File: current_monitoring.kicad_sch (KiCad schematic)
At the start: 0 parts

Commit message: moving laptops
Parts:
- added R37: 28m, symbol Device:R
- added R38: 53m, symbol Device:R
- added R39: 1.1k, symbol Device:R
- added R40: 2.4k, symbol Device:R
- added U2: INA2180, symbol utsvt-chips:INA2180
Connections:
- net 12V_IN: now also R37.1, U2.2 (IN-)
- net 5V_IN: now also R38.1, U2.6 (IN-)
- new net: R39.1, U2.1 (OUT)
- new net: R39.2, R40.1
- new net 12V_LOAD: R37.2, U2.3 (IN+)
- new net 5V_LOAD: R38.2, U2.5 (IN+), U2.8 (VS), U2.8 (VS)
- new net GND: R40.2, U2.4 (GND), U2.4 (GND)

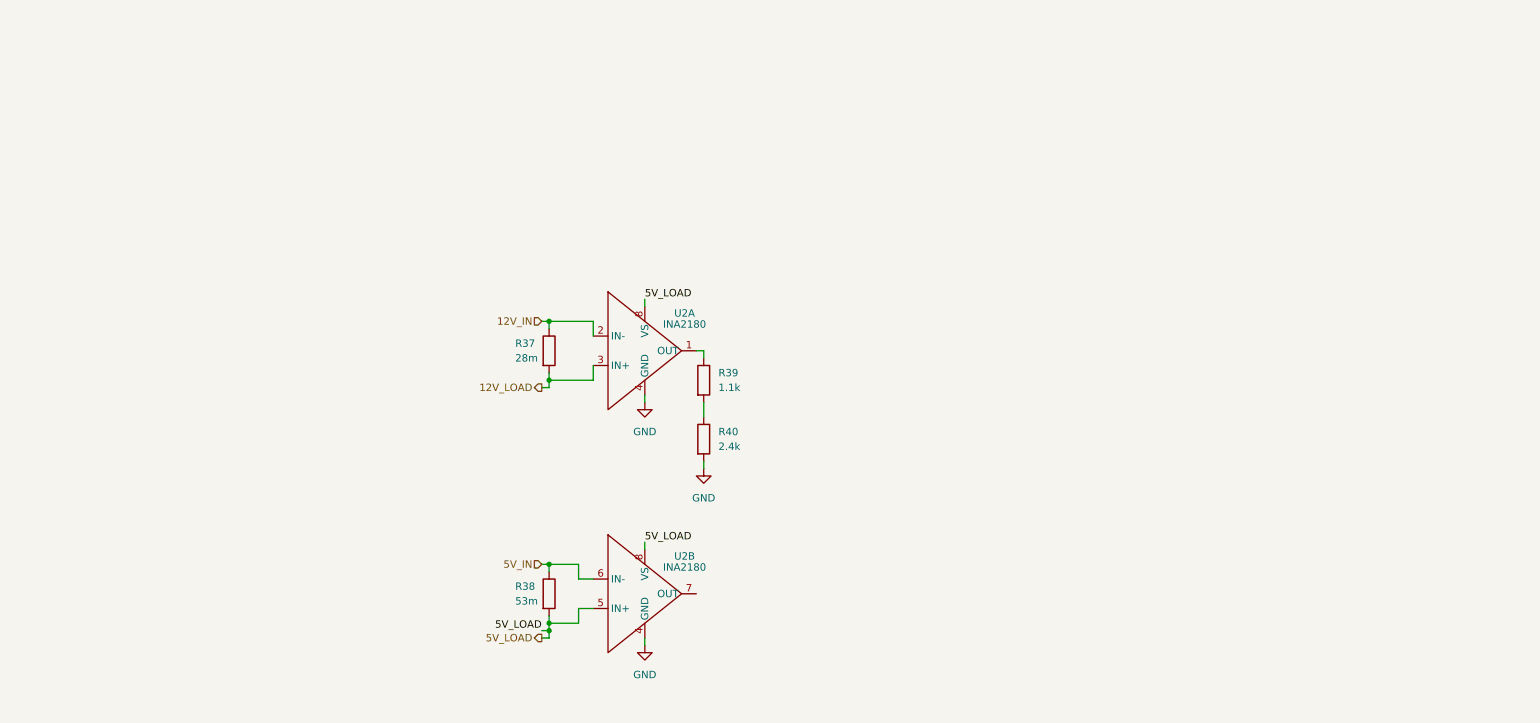
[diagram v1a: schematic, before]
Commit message: initial draft w/ current sense for 5V
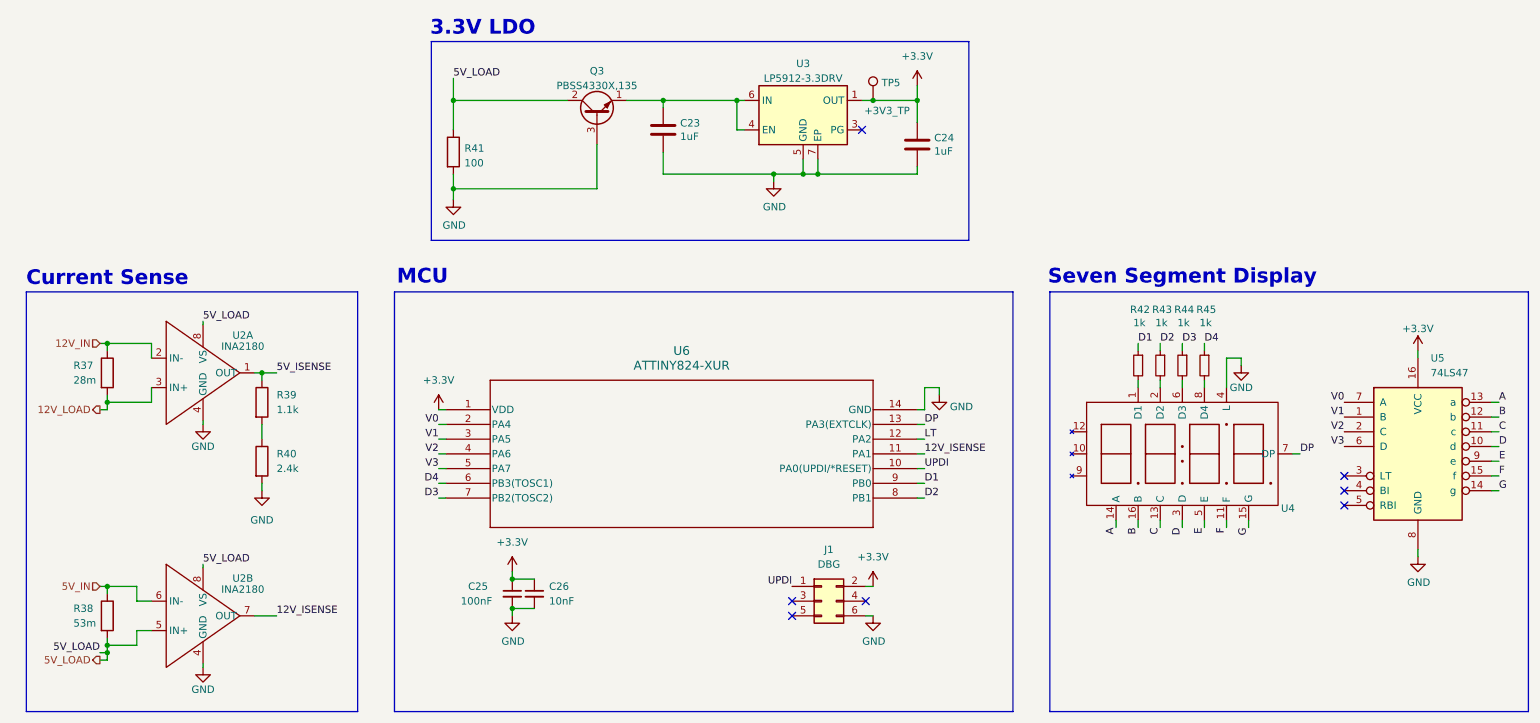
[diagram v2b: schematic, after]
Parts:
- added C23, C24: 1uF, Capacitor_SMD:C_0805_2012Metric, symbol Device:C
- added C25: 100nF, symbol Device:C_Small
- added C26: 10nF, symbol Device:C_Small
- added J1: DBG, symbol Connector_Generic:Conn_02x03_Odd_Even
- added Q3: PBSS4330X,135, Package_TO_SOT_SMD:SOT-89-3, symbol Transistor_BJT:2SC1815
- added R41: 100, Resistor_SMD:R_0805_2012Metric, symbol Device:R
- added R42, R43, R44, R45: 1k, symbol Device:R_Small
- added TP5: +3V3_TP, Connector_PinHeader_2.54mm:PinHeader_1x01_P2.54mm_Vertical, symbol Connector:TestPoint
- added U3: LP5912-3.3DRV, Package_SON:WSON-6-1EP_2x2mm_P0.65mm_EP1x1.6mm, symbol Regulator_Linear:LP5912-3.3DRV
- added U4: ~, symbol utsvt-misc:LTC-4627JS
- added U5: 74LS47, symbol 74xx:74LS47
- added U6: ATTINY824-XUR, TSSOP14_ST_MCH, symbol utsvt-microcontrollers:ATTINY824-XUR
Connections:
- net 5V_LOAD: now also Q3.2 (C), R41.1
- net GND: now also C23.2, C24.2, C25.2, C26.2, J1.6 (Pin_6), Q3.3 (B), R41.2, U3.5 (GND), U3.7 (EP), U4.4 (L), U5.8 (GND), U6.14 (GND)
- net 5V_ISENSE: now reaches R39.1, U2.1 (OUT)
- net 12V_ISENSE: now reaches U2.7 (OUT)
- net 12V_ISENSE: now also U6.11 (PA1)
- new net: R42.2, U4.1 (D1)
- new net: R43.2, U4.2 (D2)
- new net: R44.2, U4.6 (D3)
- new net: R45.2, U4.8 (D4)
- new net: C23.1, Q3.1 (E), U3.4 (EN), U3.6 (IN)
- new net +3.3V: C24.1, C25.1, C26.1, J1.2 (Pin_2), TP5.1, U3.1 (OUT), U5.16 (VCC), U6.1 (VDD)
- new net A: U4.14 (A), U5.13 (a)
- new net B: U4.16 (B), U5.12 (b)
- new net C: U4.13 (C), U5.11 (c)
- new net D: U4.3 (D), U5.10 (d)
- new net D1: R42.1, U6.9 (PB0)
- new net D2: R43.1, U6.8 (PB1)
- new net D3: R44.1, U6.7 (PB2(TOSC2))
- new net D4: R45.1, U6.6 (PB3(TOSC1))
- new net DP: U4.7 (DP), U6.13 (PA3(EXTCLK))
- new net E: U4.5 (E), U5.9 (e)
- new net F: U4.11 (F), U5.15 (f)
- new net G: U4.15 (G), U5.14 (g)
- new net LT: U6.12 (PA2)
- new net UPDI: J1.1 (Pin_1), U6.10 (PA0(UPDI/*RESET))
- new net V0: U5.7 (A), U6.2 (PA4)
- new net V1: U5.1 (B), U6.3 (PA5)
- new net V2: U5.2 (C), U6.4 (PA6)
- new net V3: U5.6 (D), U6.5 (PA7)
- no-connect marks 0 -> 7
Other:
- note added: "3.3V LDO"
- note added: "Current Sense"
- note added: "MCU"
- note added: "Seven Segment Display"
- moved on the sheet: R37, R38, R39, R40, U2A, U2B

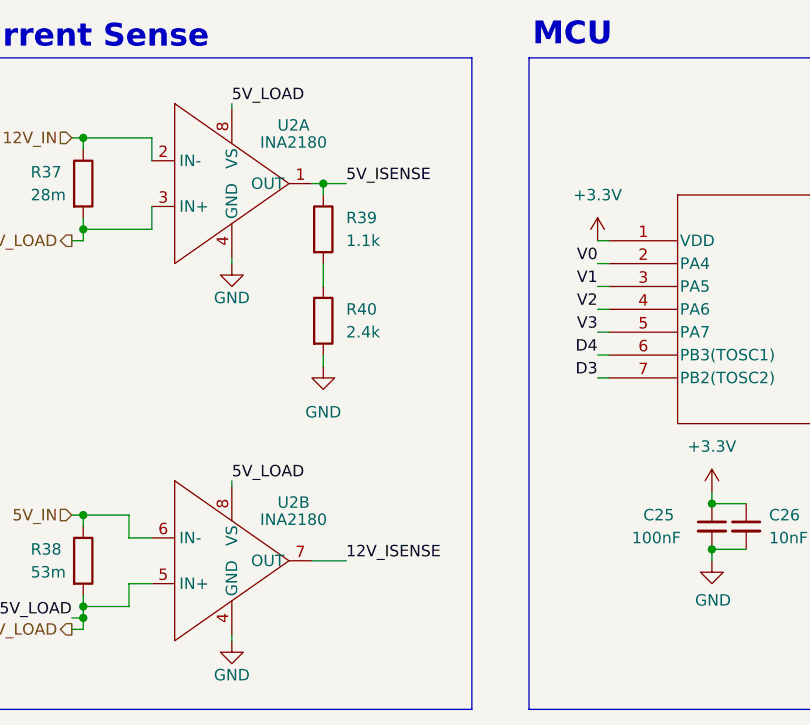
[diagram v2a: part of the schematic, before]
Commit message: accidentally flipped current sense; also routed high level schematic
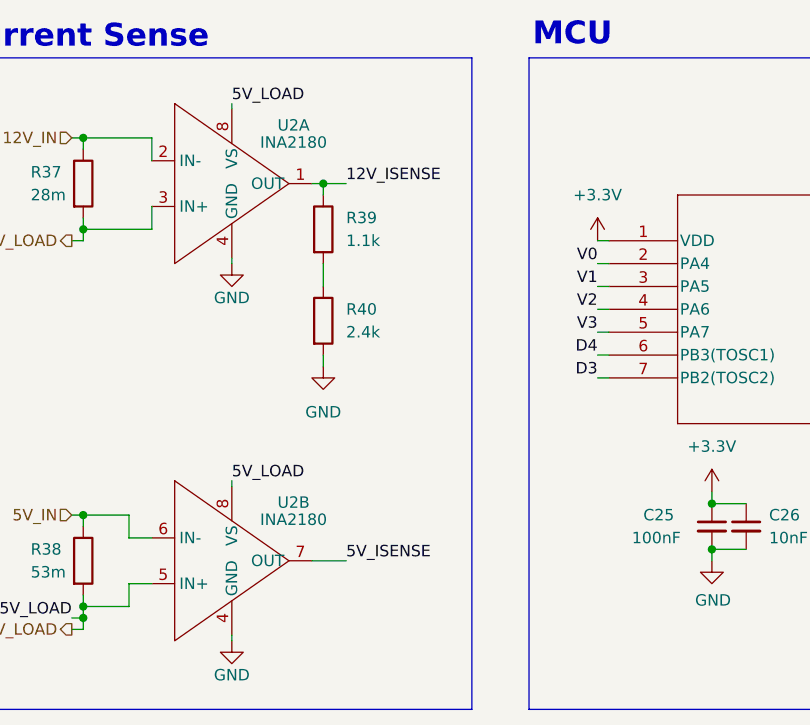
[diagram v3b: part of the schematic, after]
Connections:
- net 12V_ISENSE: now also R39.1, U2.1 (OUT); no longer U2.7 (OUT)
- net 5V_ISENSE: now also U2.7 (OUT); no longer R39.1, U2.1 (OUT)
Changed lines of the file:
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@@
 	)
 	(label "12V_ISENSE"
-		(at 63.5 125.73 0)
+		(at 63.5 83.82 0)
 		(fields_autoplaced yes)
 		(effects
@@
 	)
 	(label "5V_ISENSE"
-		(at 63.5 83.82 0)
-		(fields_autoplaced yes)
-		(effects
+		(at 63.5 125.73 0)
+		(fields_autoplaced yes)
+		(effects

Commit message: finished first draft
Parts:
- removed R38: 53m, symbol Device:R
- removed unit 2 of U2

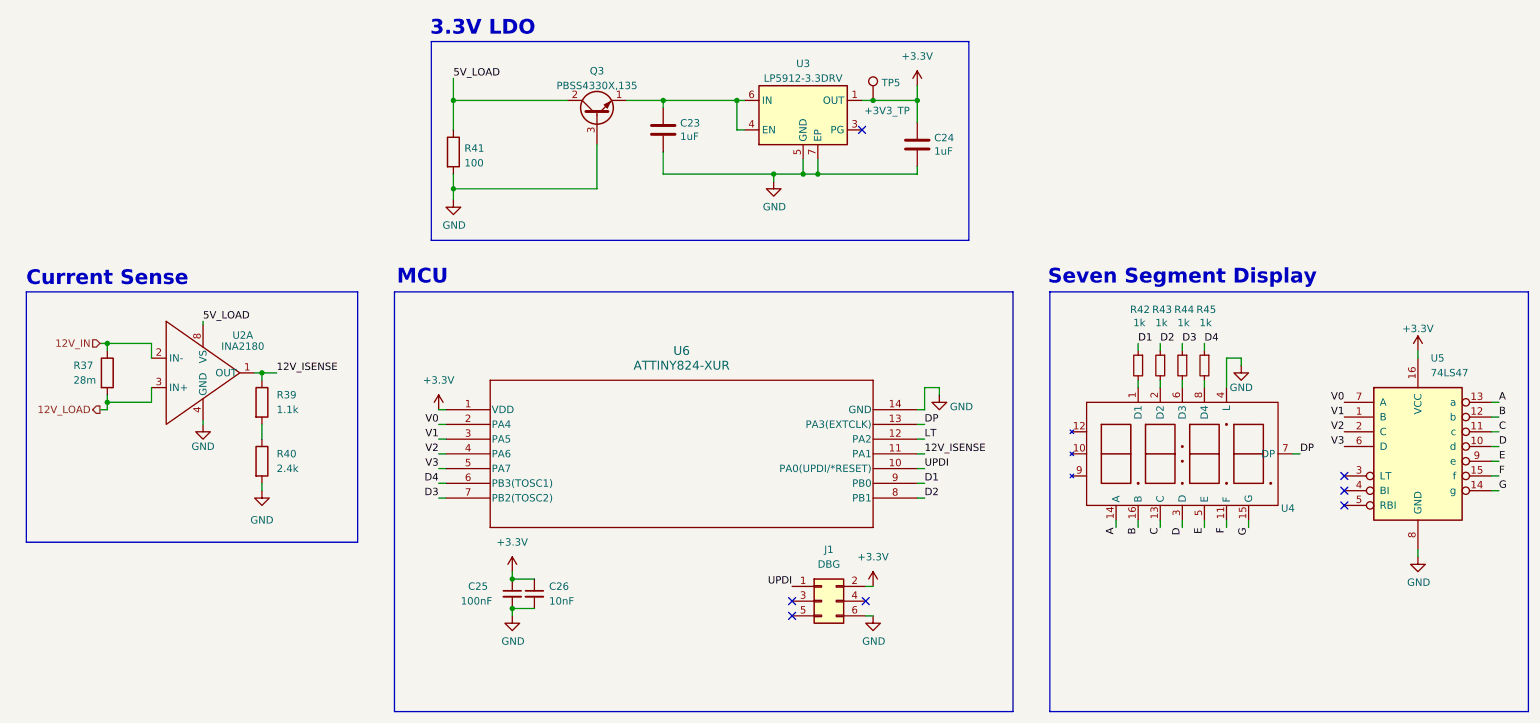
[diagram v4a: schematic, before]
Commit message: changed to 1-channel chip for current sense & fixed ERC
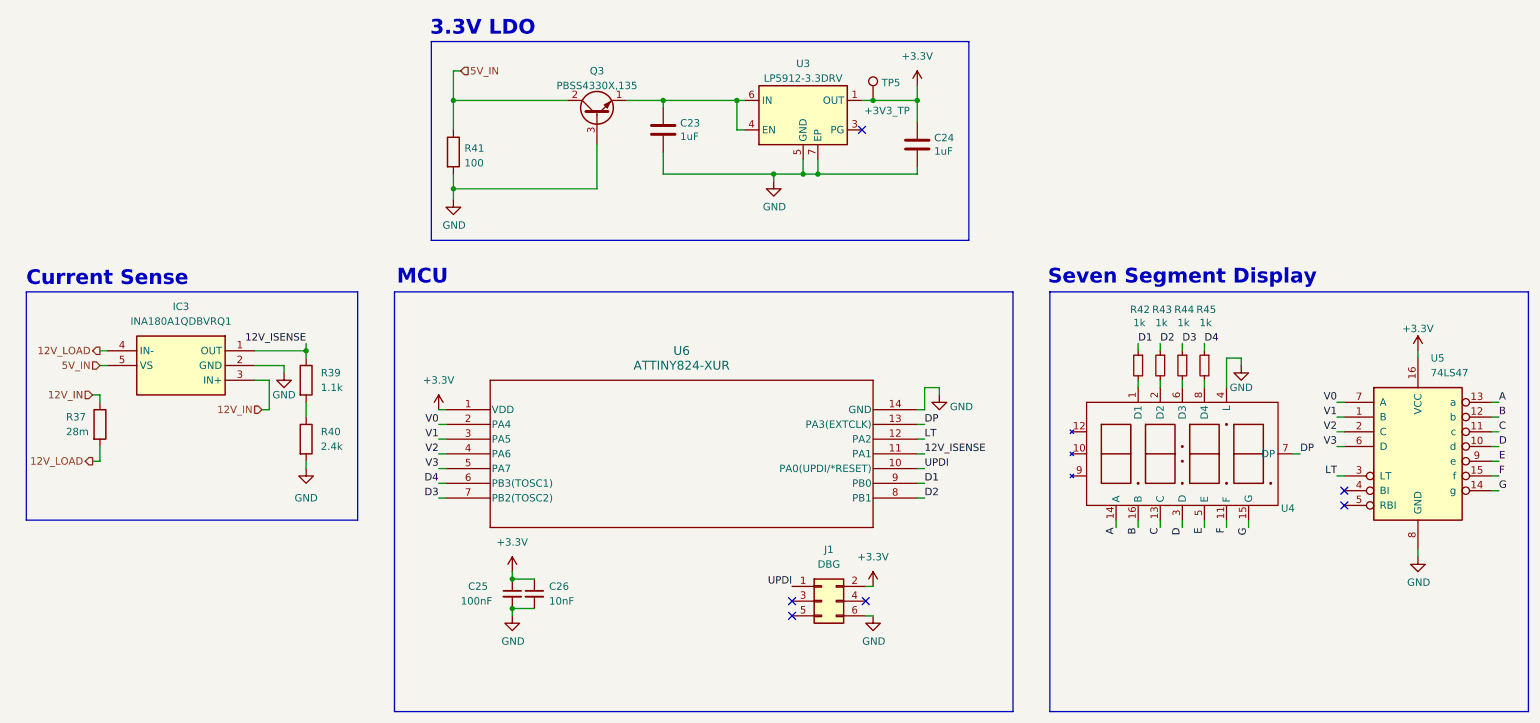
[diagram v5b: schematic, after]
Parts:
- removed U2: INA2180, symbol utsvt-chips:INA2180
- added IC3: INA180A1QDBVRQ1, SOT95P280X145-5N, symbol utsvt-chips:INA180A1QDBVRQ1
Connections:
- net 12V_IN: now also IC3.3 (IN+)
- net 12V_ISENSE: now also IC3.1 (OUT)
- net 12V_LOAD: now also IC3.4 (IN-)
- net GND: now also IC3.2 (GND)
- net LT: now also U5.3 (LT)
- net 5V_LOAD renamed 5V_IN
- net 5V_IN: now also IC3.5 (VS)
- no-connect marks 7 -> 6
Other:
- moved on the sheet: R37, R39, R40

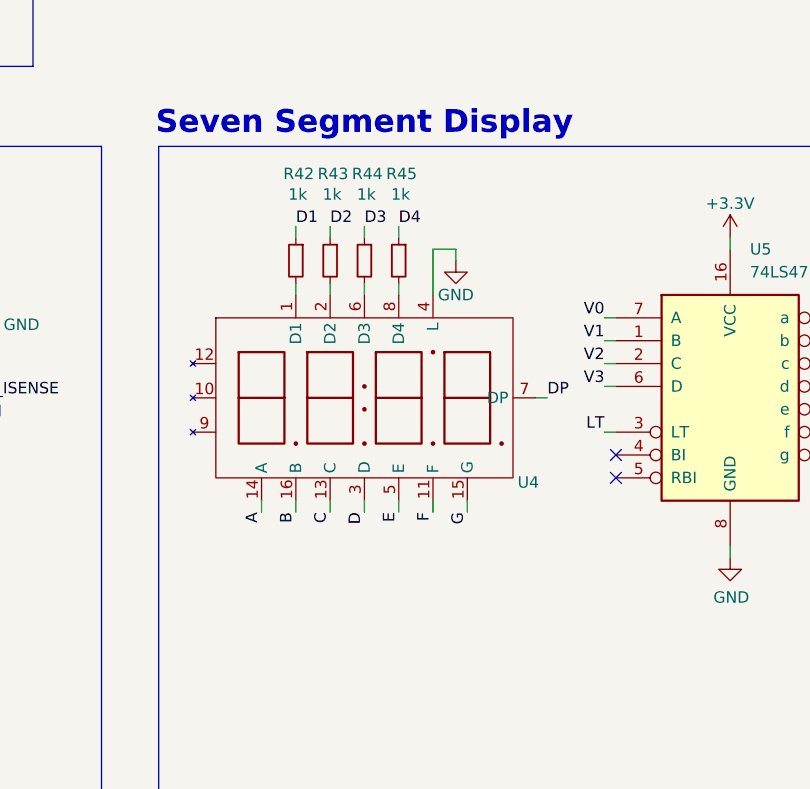
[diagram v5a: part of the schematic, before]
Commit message: added proper current limiting resistors for 2mA on seven seg
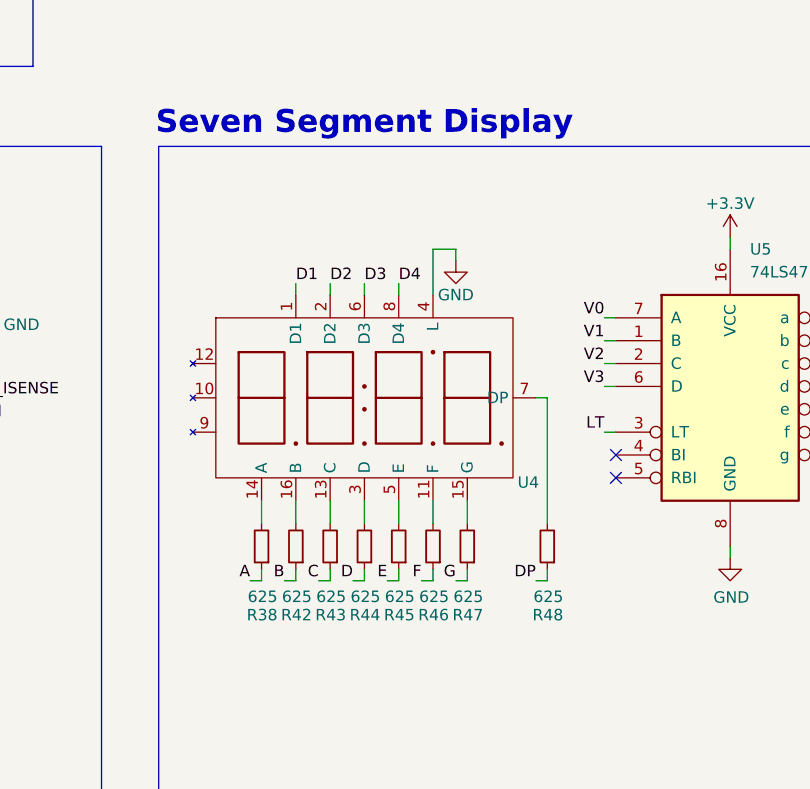
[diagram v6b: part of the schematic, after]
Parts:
- added R38, R46, R47, R48: 625, symbol Device:R_Small
- R42, R43, R44, R45: value 1k -> 625
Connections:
- net A: now also R38.1; no longer U4.14 (A)
- net B: now also R42.1; no longer U4.16 (B)
- net C: now also R43.1; no longer U4.13 (C)
- net D: now also R44.1; no longer U4.3 (D)
- net D1: now also U4.1 (D1); no longer R42.1
- net D2: now also U4.2 (D2); no longer R43.1
- net D3: now also U4.6 (D3); no longer R44.1
- net D4: now also U4.8 (D4); no longer R45.1
- net DP: now also R48.1; no longer U4.7 (DP)
- net E: now also R45.1; no longer U4.5 (E)
- net F: now also R46.1; no longer U4.11 (F)
- net G: now also R47.1; no longer U4.15 (G)
- net at R42.2: now also U4.16 (B); no longer U4.1 (D1)
- net at R43.2: now also U4.13 (C); no longer U4.2 (D2)
- net at R44.2: now also U4.3 (D); no longer U4.6 (D3)
- net at R45.2: now also U4.5 (E); no longer U4.8 (D4)
- new net: R46.2, U4.11 (F)
- new net: R38.2, U4.14 (A)
- new net: R47.2, U4.15 (G)
- new net: R48.2, U4.7 (DP)
